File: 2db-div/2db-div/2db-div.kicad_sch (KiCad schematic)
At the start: 24 parts

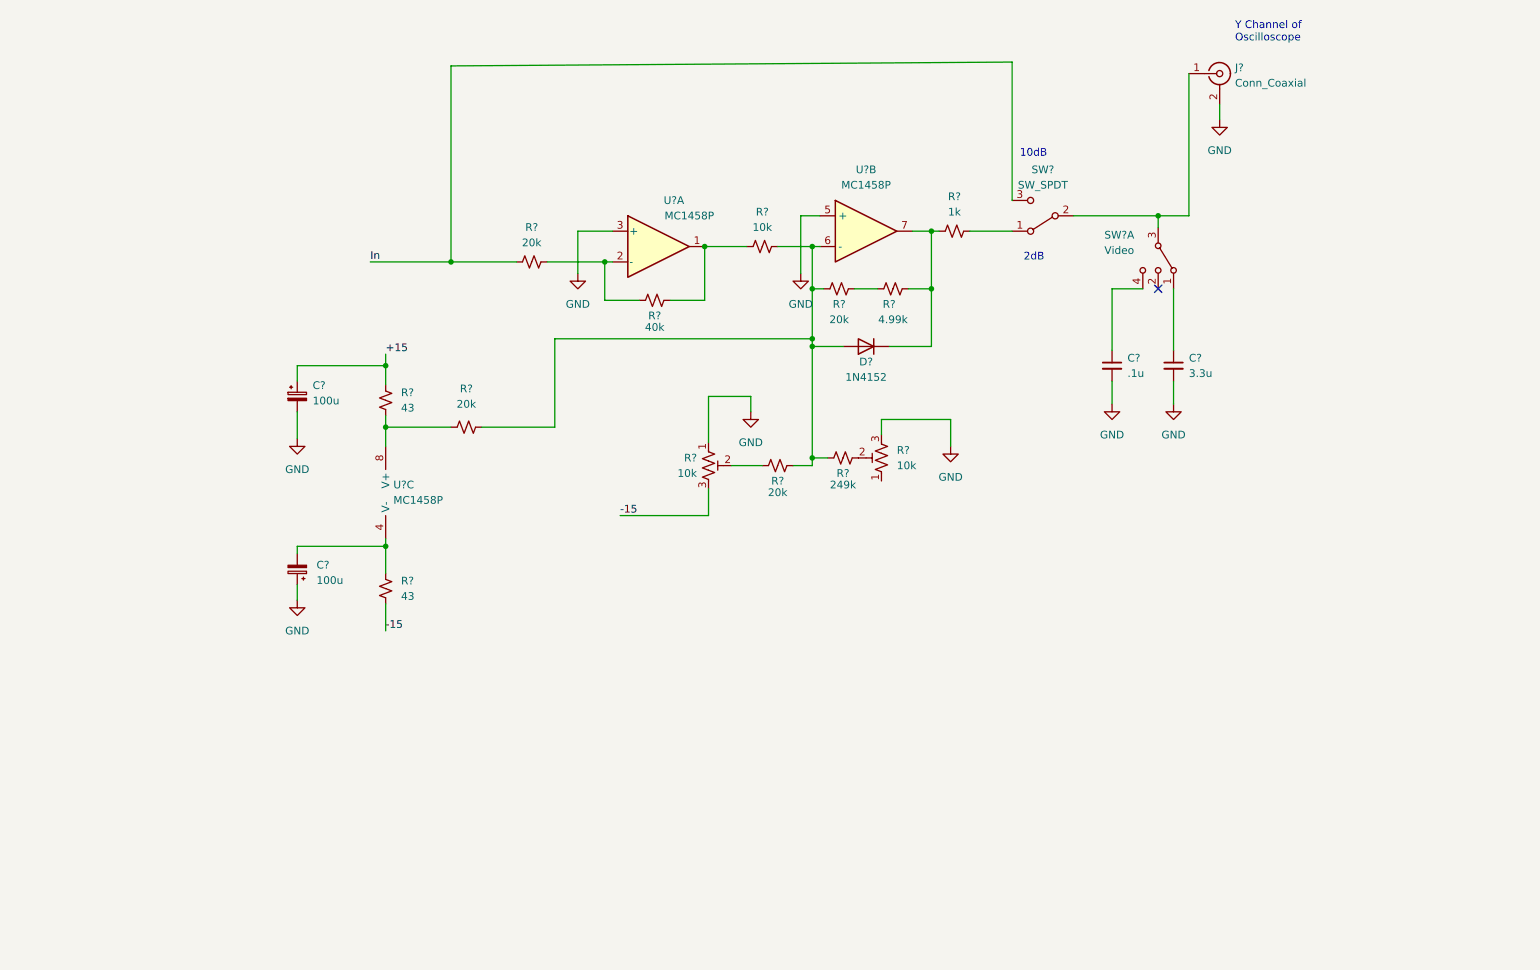
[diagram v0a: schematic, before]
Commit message: add annotations to 2db-div schematic
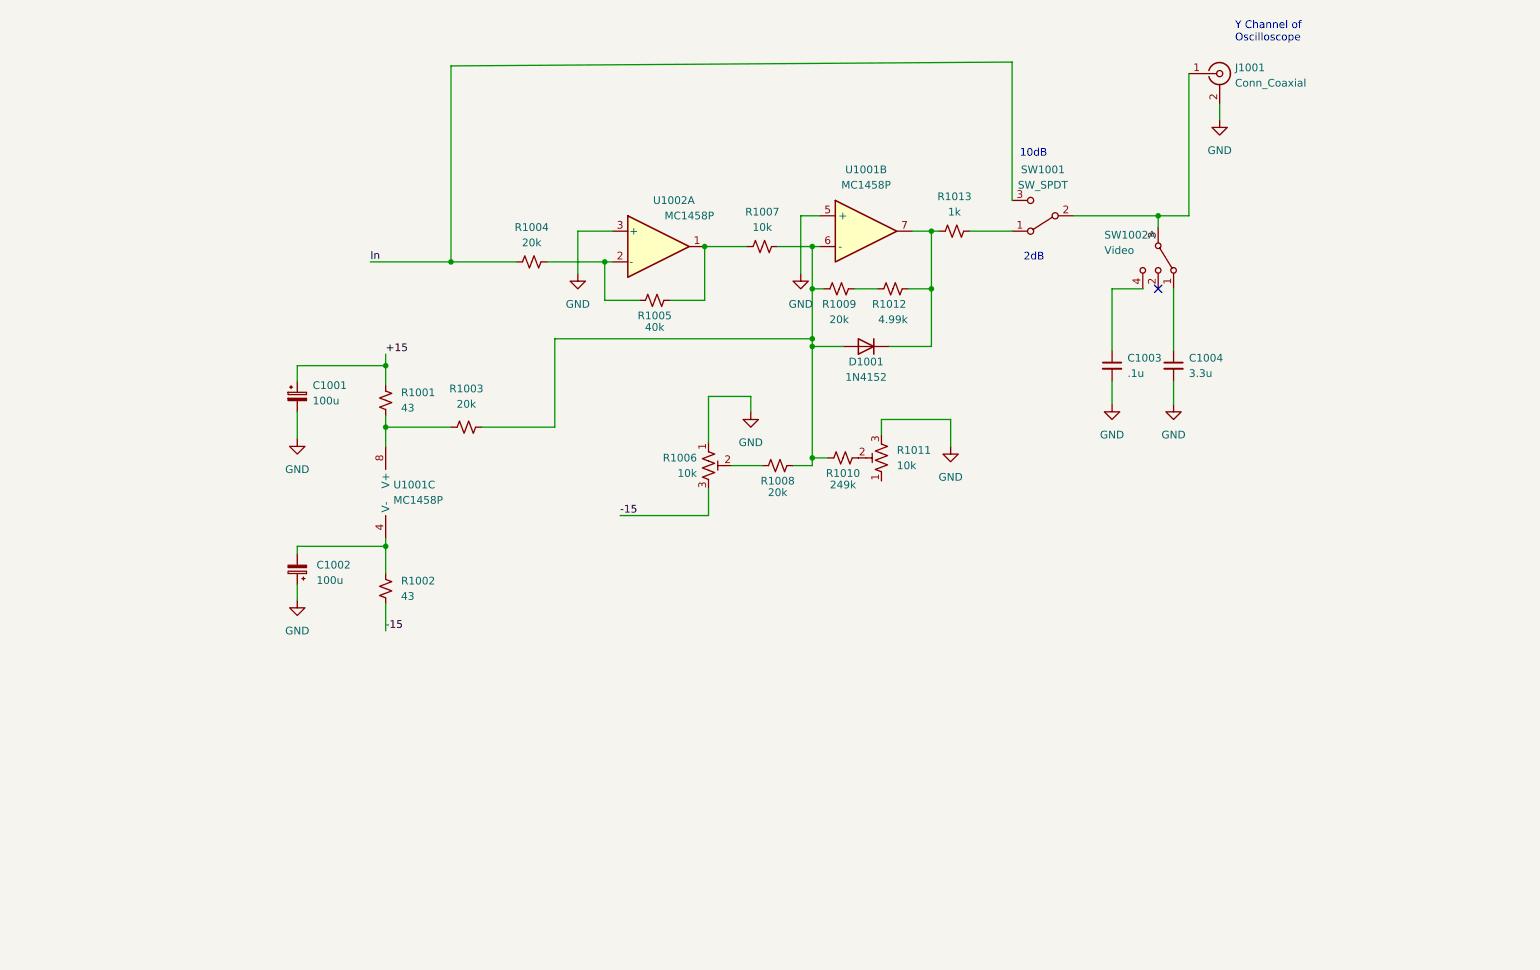
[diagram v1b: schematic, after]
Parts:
- gave numbers to parts that had none: 23

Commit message: improved if and log amp and second lo/mixer
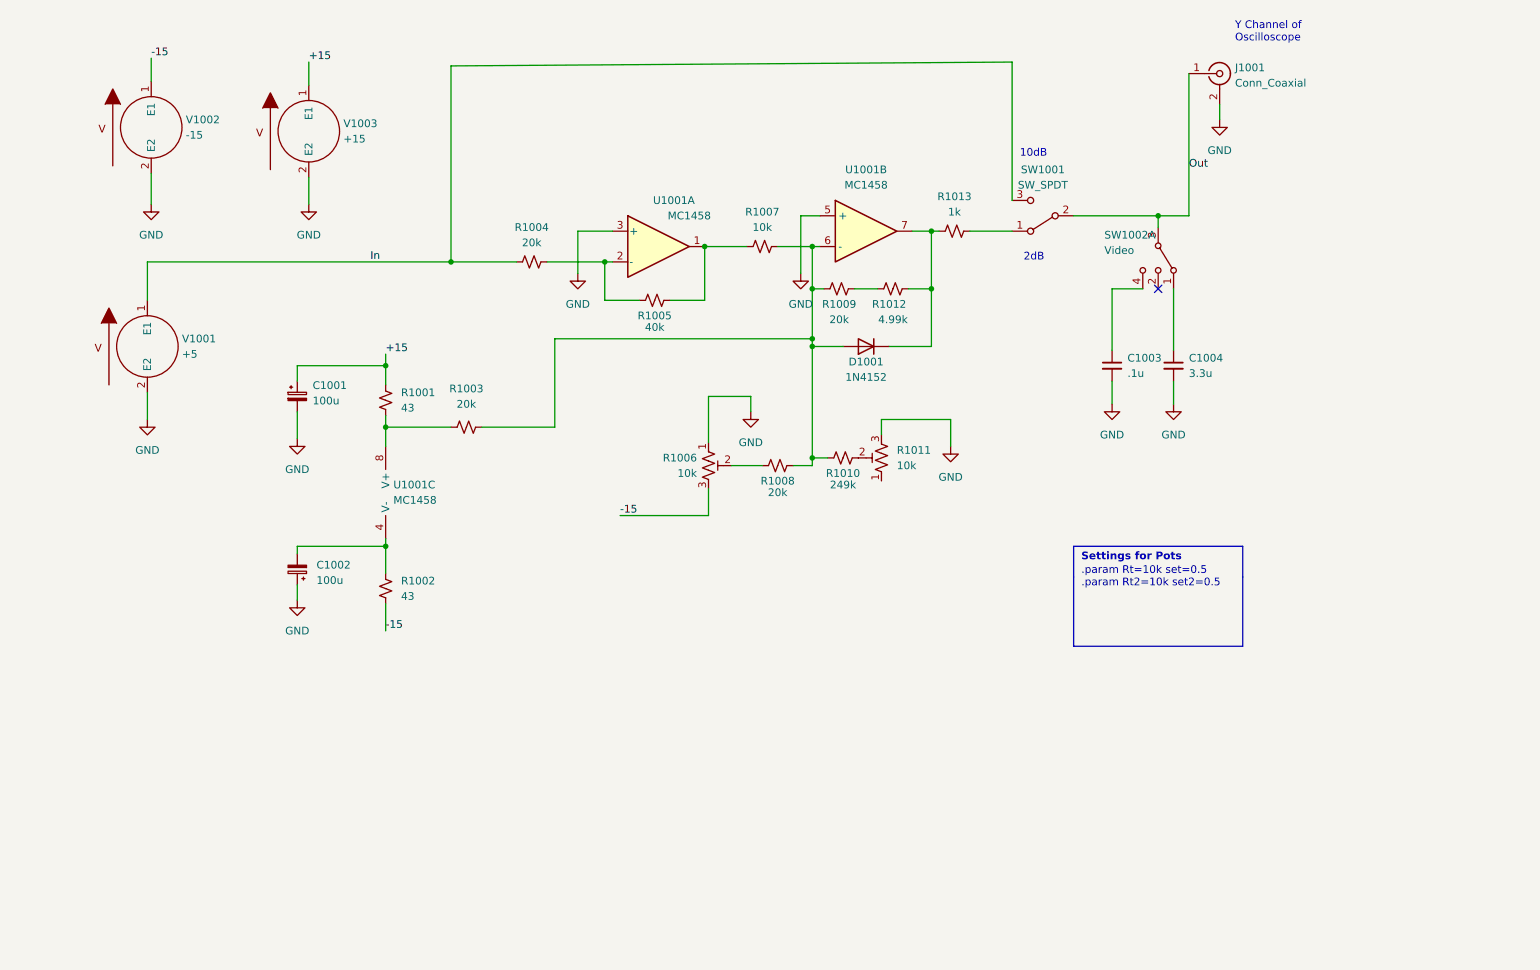
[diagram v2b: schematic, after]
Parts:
- added V1001: +5, symbol pspice:VSOURCE
- added V1002: -15, symbol pspice:VSOURCE
- added V1003: +15, symbol pspice:VSOURCE
- D1001: Spice_Lib_File (none) -> 2db-div-spice\fairch.lib; Spice_Model (none) -> 1N4152; Spice_Netlist_Enabled (none) -> Y; Spice_Node_Sequence (none) -> 2 1; Spice_Primitive (none) -> D
- J1001: Spice_Model (none) -> Conn_Coaxial; Spice_Netlist_Enabled (none) -> N; Spice_Primitive (none) -> J
- R1006: Spice_Lib_File (none) -> 2db-div-spice\Pot.lib; Spice_Model (none) -> pot_lin; Spice_Netlist_Enabled (none) -> Y; Spice_Primitive (none) -> X
- R1011: Spice_Lib_File (none) -> 2db-div-spice\Pot2.lib; Spice_Model (none) -> pot_lin2; Spice_Netlist_Enabled (none) -> Y; Spice_Primitive (none) -> X
- SW1001: Spice_Netlist_Enabled (none) -> N; Spice_Primitive (none) -> R
- U1001: renamed from U1002; value MC1458P -> MC1458; Spice_Lib_File (none) -> 2db-div-spice\MC1458-dual.lib; Spice_Model (none) -> MC1458_ti; Spice_Netlist_Enabled (none) -> Y; Spice_Primitive (none) -> X
- U1001: value MC1458P -> MC1458; Spice_Lib_File (none) -> 2db-div-spice\MC1458-dual.lib; Spice_Model (none) -> MC1458_ti; Spice_Netlist_Enabled (none) -> Y; Spice_Primitive (none) -> X
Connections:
- net +15: now also V1003.1 (E1)
- net -15: now also V1002.1 (E1)
- net GND: now also V1001.2 (E2), V1002.2 (E2), V1003.2 (E2)
- net In: now also V1001.1 (E1)
- net Out: now reaches J1001.1 (In), SW1001.2 (B), SW1002.3
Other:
- note added: ".param Rt=10k set=0.5 .param Rt2=10k set2=0.5"
- note added: "Settings for Pots"

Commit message: 2db-div layout
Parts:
- added H1001, H1002, H1003, H1004: MountingHole, MountingHole:MountingHole_3.2mm_M3, symbol Mechanical:MountingHole
- added J1001, J1003: Conn_01x02, 2db-div:691103110002, symbol Connector_Generic:Conn_01x02
- added J1002: From R2, Connector_Wire:SolderWire-0.5sqmm_1x01_D0.9mm_OD2.1mm, symbol Connector:Conn_01x01_Female
- added TP1001, TP1002: TestPoint, TestPoint:TestPoint_Pad_1.0x1.0mm, symbol Connector:TestPoint_Probe
- C1001, C1002: footprint (none) -> Capacitor_THT:CP_Radial_D5.0mm_P2.50mm
- J1004: renamed from J1001; footprint (none) -> Connector_Wire:SolderWire-0.5sqmm_1x02_P4.6mm_D0.9mm_OD2.1mm
- R1001, R1002, R1003, R1004, R1005, R1007, R1008, R1009, R1010, R1013: footprint (none) -> Resistor_THT:R_Axial_DIN0207_L6.3mm_D2.5mm_P7.62mm_Horizontal
- R1006: footprint (none) -> 2db-div:TRIM_3362P-1-103LF
- R1011: renamed from R1012; footprint (none) -> Resistor_THT:R_Axial_DIN0207_L6.3mm_D2.5mm_P7.62mm_Horizontal
- R1012: renamed from R1011; footprint (none) -> 2db-div:TRIM_3362P-1-103LF
- U1001: footprint (none) -> 2db-div:MC1458P
- V1001, V1002, V1003: now left out of the parts list
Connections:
- net +15: now also J1001.1 (Pin_1)
- net -15: now also R1012.1, J1003.1 (Pin_1)
- net GND: now also J1001.2 (Pin_2), J1003.2 (Pin_2)
- net In: now also J1002.1 (Pin_1)
- net at R1005.2, R1007.1, U1001.1: now also TP1001.1
- net at D1001.1 (K), R1011.2, R1013.1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: now also TP1002.1
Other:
- moved on the sheet: C1001, C1002, C1003, C1004, D1001, J1004, R1001, R1002, R1003, R1004, R1005, R1006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
